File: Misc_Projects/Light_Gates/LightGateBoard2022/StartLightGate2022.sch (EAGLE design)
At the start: 6 parts

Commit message: Light Gate Updates
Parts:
- removed IC1: (no value), GTOR - Active Components:REG_5V_L7805_VERT
- removed X1: (no value), GTOR - Microfit Connector:HEADER_POS6_43045-0600
- added IC2: (no value), GTOR - Active Components:REG_5V_L7805_HOR
- added JP1: (no value), GTOR - Connectors:PINHD-1X6
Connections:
- net +3V3: now also JP1.6; no longer X1.6
- net +5V: now also IC2.OUT; no longer IC1.OUT
- net GND: now also IC2.GND, JP1.5; no longer IC1.GND, X1.5
- net INT: now also JP1.1; no longer X1.1
- net SCL: now also JP1.3; no longer X1.3
- net SDA: now also JP1.4; no longer X1.4
- net SHUT: now also JP1.2; no longer X1.2
- net VCC: now also IC2.IN; no longer IC1.IN

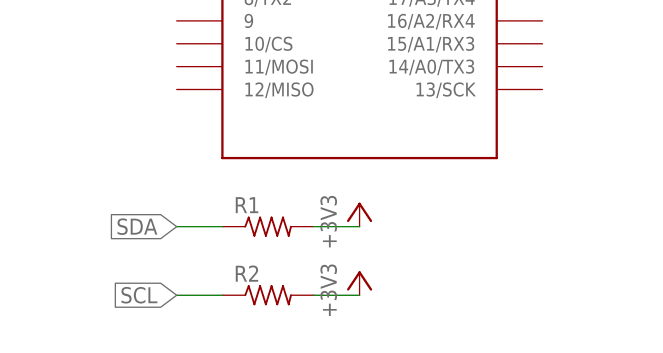
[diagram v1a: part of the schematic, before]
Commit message: Fixeed light gate start board
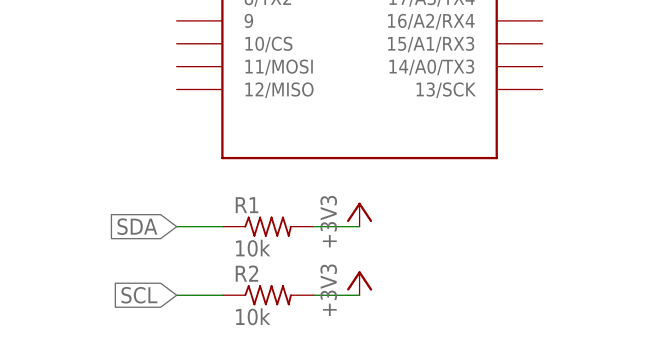
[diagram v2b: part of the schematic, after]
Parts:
- R1, R2: value (none) -> 10k
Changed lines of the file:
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@@
 <part name="+3V1" library="GTOR - Documation Frame" deviceset="+3V3" device=""/>
 <part name="P+2" library="GTOR - Documation Frame" deviceset="VCC" device=""/>
-<part name="R1" library="GTOR - Passive Components" deviceset="RES_AXIAL" device="1/4W-0.4" package3d_urn="urn:adsk.eagle:package:23491/2"/>
-<part name="R2" library="GTOR - Passive Components" deviceset="RES_AXIAL" device="1/4W-0.4" package3d_urn="urn:adsk.eagle:package:23491/2"/>
+<part name="R1" library="GTOR - Passive Components" deviceset="RES_AXIAL" device="1/4W-0.4" package3d_urn="urn:adsk.eagle:package:23491/2" value="10k"/>
+<part name="R2" library="GTOR - Passive Components" deviceset="RES_AXIAL" device="1/4W-0.4" package3d_urn="urn:adsk.eagle:package:23491/2" value="10k"/>
 <part name="+3V3" library="GTOR - Documation Frame" deviceset="+3V3" device=""/>
 <part name="+3V4" library="GTOR - Documation Frame" deviceset="+3V3" device=""/>
